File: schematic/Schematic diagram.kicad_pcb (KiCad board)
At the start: 2 copper layers, 23 parts, among them U1 MP4050

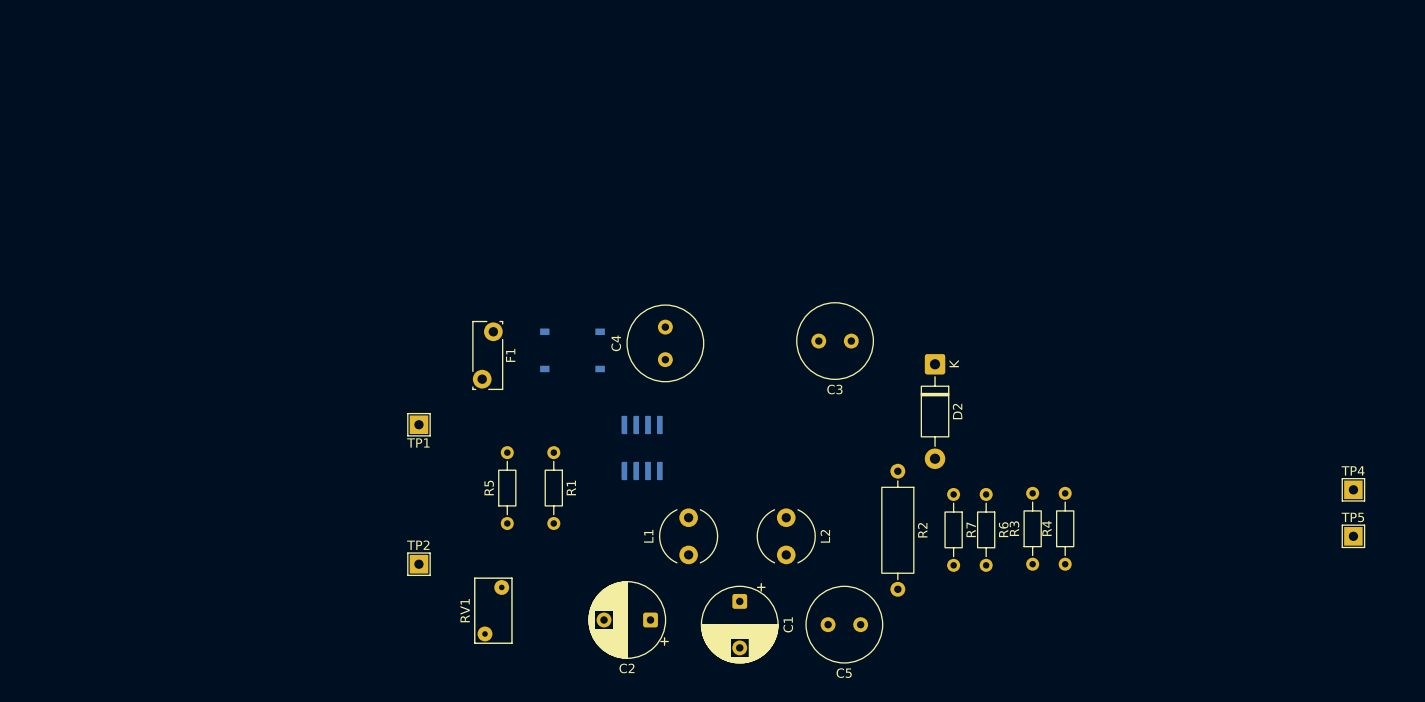
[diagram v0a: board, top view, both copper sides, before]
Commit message: Update PCB routing and improve .gitignore
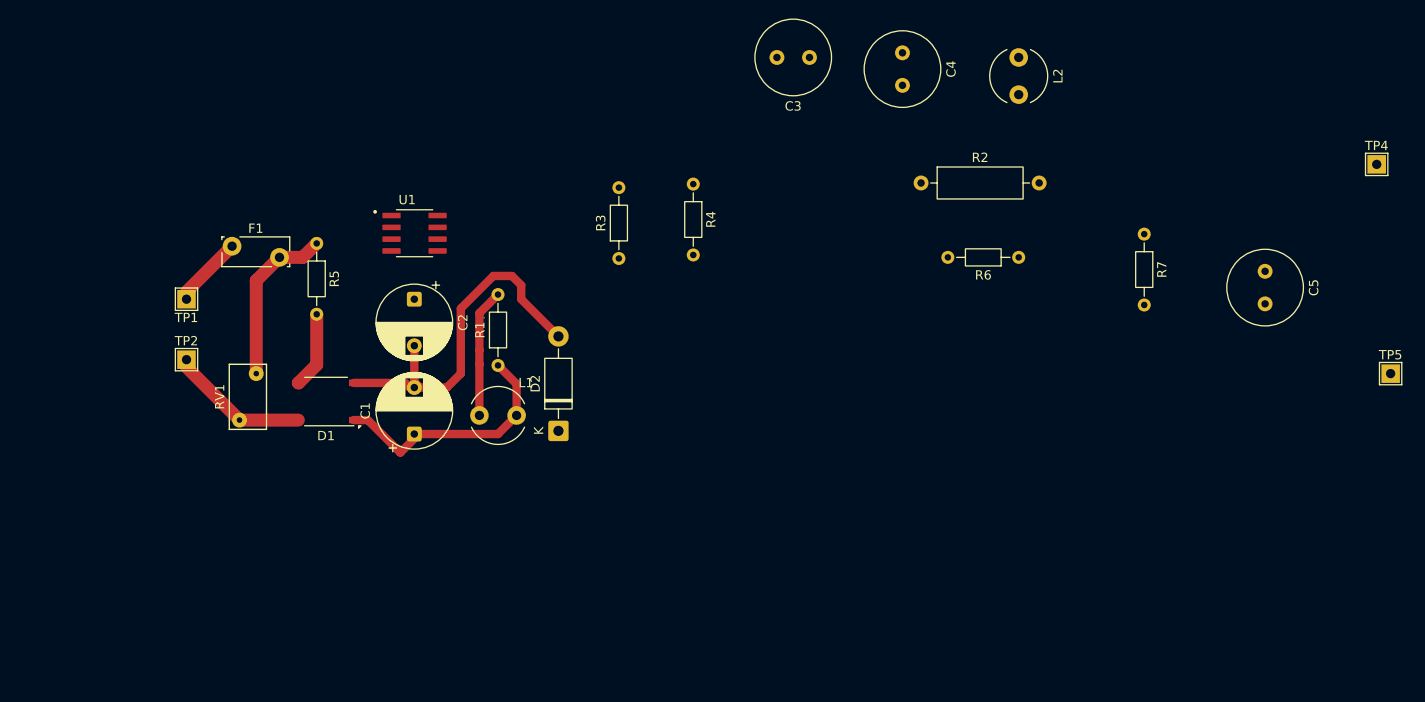
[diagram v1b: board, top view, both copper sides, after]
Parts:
- D1, U1: moved to F.Cu
- moved C5 57.8 mm to (178.0, 93.5), turned to -90 degrees
- moved R4 57.2 mm to (116.5, 84.1), turned to -90 degrees
- moved L2 55.5 mm to (151.5, 70.5)
- moved R3 55.3 mm to (108.5, 92.1)
- moved C2 42.8 mm to (86.5, 96.5), turned to -90 degrees
- moved C4 41.7 mm to (139.0, 70.0), turned to -90 degrees
- moved D2 41.1 mm to (102.0, 110.7), turned to 90 degrees
- moved C1 39.4 mm to (86.5, 111.0), turned to 90 degrees
- moved R5 36.4 mm to (76.0, 90.5), turned to -90 degrees
- moved TP4 35.1 mm to (190.0, 82.0)
- moved RV1 35.0 mm to (69.5, 104.5)
- moved R7 34.7 mm to (165.0, 89.5)
- moved U1 33.7 mm to (86.5, 89.4), turned to 0 degrees
- moved TP2 33.3 mm to (62.0, 103.0)
- moved R2 31.1 mm to (141.0, 84.0), turned to 0 degrees
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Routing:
- net Net-(D1--): track 0.00 -> 41.2 mm
- net Net-(D1-+): track 0.00 -> 27.3 mm
- net Net-(F1-Pad2): track 0.00 -> 18.2 mm
- net Net-(D1-Pad4): track 0.00 -> 15.2 mm
- net Net-(U1-DRAIN): track 0.00 -> 14.3 mm
- net Net-(D1-Pad3): track 0.00 -> 8.21 mm
- net Net-(F1-Pad1): track 0.00 -> 7.73 mm

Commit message: Update PCB routing and add LED schematic, layout and 3D images
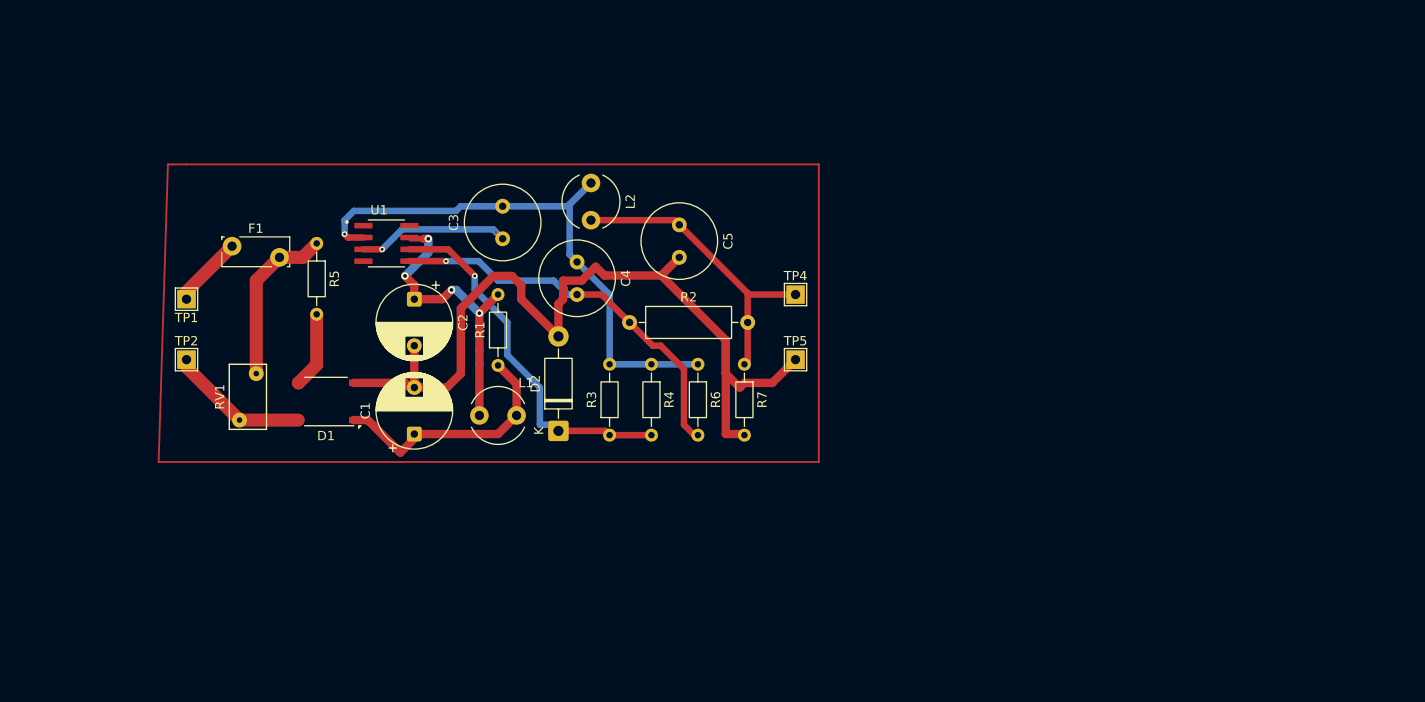
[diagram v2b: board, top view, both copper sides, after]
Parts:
- moved TP4 64.0 mm to (127.5, 96.0)
- moved TP5 64.0 mm to (127.5, 103.0)
- moved C5 63.2 mm to (115.0, 88.5)
- moved L2 47.9 mm to (105.5, 84.0)
- moved R7 45.2 mm to (122.0, 103.5)
- moved C4 41.6 mm to (104.0, 92.5)
- moved C3 38.3 mm to (96.0, 90.0), turned to 90 degrees
- moved R6 36.4 mm to (117.0, 103.5), turned to -90 degrees
- moved R2 34.8 mm to (109.7, 99.0)
- moved R4 19.9 mm to (112.0, 103.5)
- moved R3 19.0 mm to (107.5, 111.1)
- moved U1 3.22 mm to (83.5, 90.5)
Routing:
- net Net-(U1-GND): track 0.00 -> 63.6 mm, vias 0 -> 1
- net Net-(D1--): track 41.2 -> 96.7 mm
- net Net-(U1-PRO): track 0.00 -> 42.4 mm, vias 0 -> 1
- net Net-(D2-K): track 0.00 -> 39.6 mm, vias 0 -> 1
- net Net-(C5-Pad1): track 0.00 -> 33.5 mm
- net Net-(U1-DRAIN): track 14.3 -> 32.1 mm, vias 0 -> 4
- net Net-(U1-VCC): track 0.00 -> 17.3 mm, vias 0 -> 1

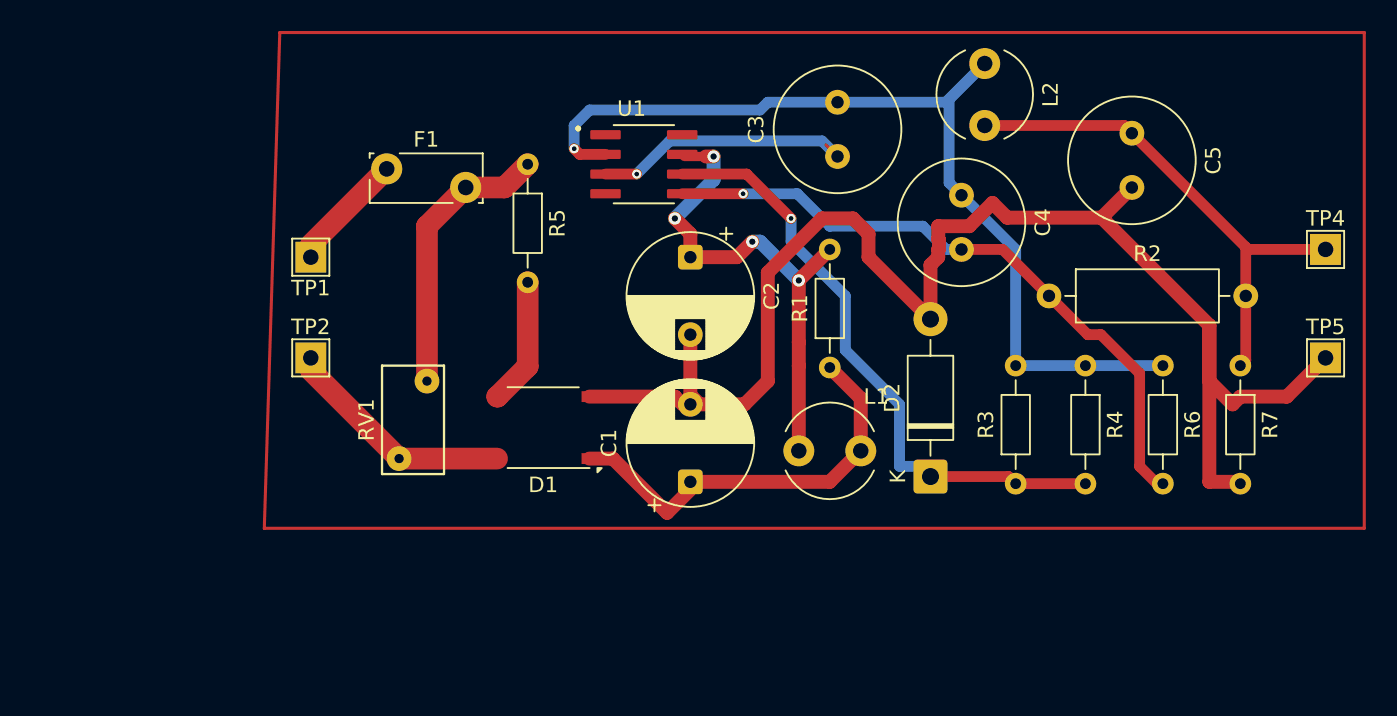
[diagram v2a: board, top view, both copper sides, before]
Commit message: Update PCB design and proteus bridge rectifier simulation
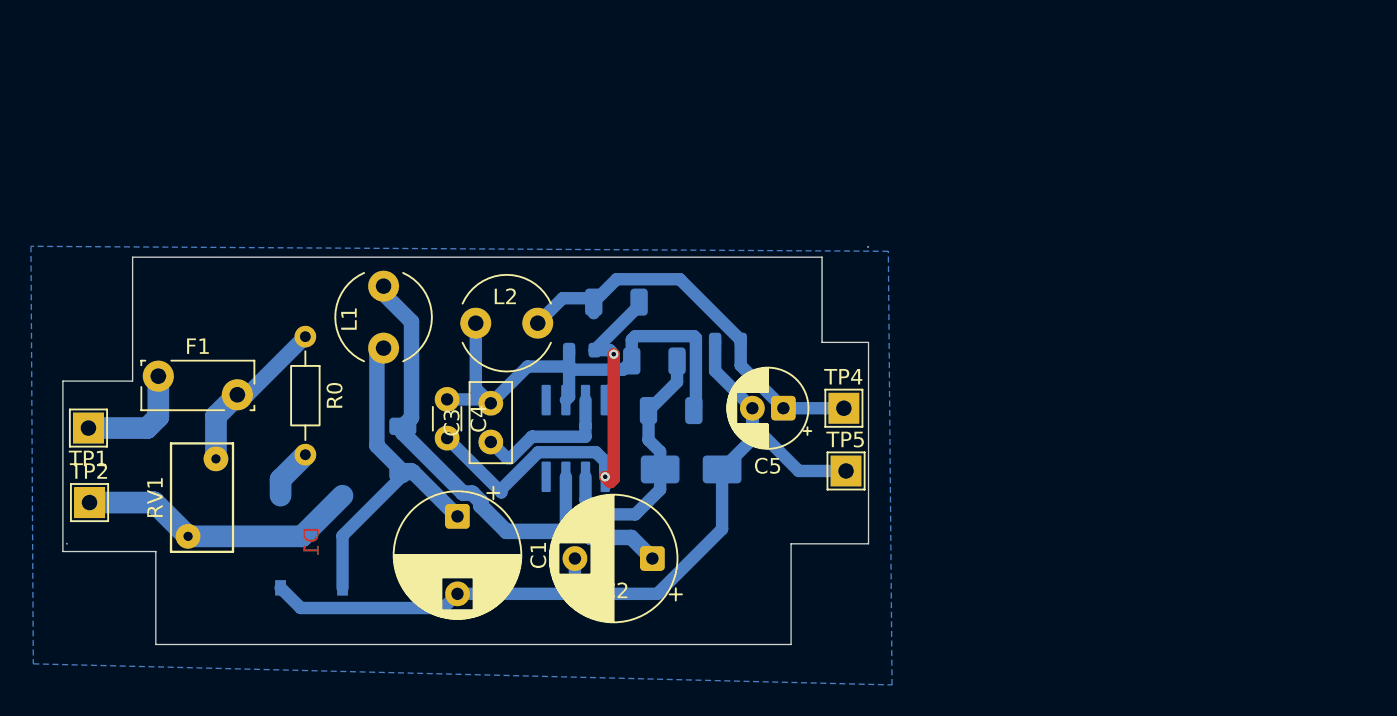
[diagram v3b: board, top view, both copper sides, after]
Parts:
- C3: footprint Capacitor_THT:C_Radial_D8.0mm_H11.5mm_P3.50mm -> Capacitor_THT:C_Disc_D5.0mm_W2.5mm_P2.50mm
- C4: footprint Capacitor_THT:C_Radial_D8.0mm_H11.5mm_P3.50mm -> Capacitor_THT:C_Disc_D3.0mm_W1.6mm_P2.50mm
- C5: footprint Capacitor_THT:C_Radial_D8.0mm_H11.5mm_P3.50mm -> Capacitor_THT:CP_Radial_D5.0mm_P2.00mm
- D1, U1: moved to B.Cu
- D2: footprint Diode_THT:D_DO-41_SOD81_P10.16mm_Horizontal -> Diode_SMD:D_SMA; moved to B.Cu
- R1: renamed from R6; footprint Resistor_THT:R_Axial_DIN0204_L3.6mm_D1.6mm_P7.62mm_Horizontal -> Resistor_SMD:R_0603_1608Metric; moved to B.Cu
- R2: footprint Resistor_THT:R_Axial_DIN0309_L9.0mm_D3.2mm_P12.70mm_Horizontal -> Resistor_SMD:R_1206_3216Metric; moved to B.Cu
- R3, R4: footprint Resistor_THT:R_Axial_DIN0204_L3.6mm_D1.6mm_P7.62mm_Horizontal -> Resistor_SMD:R_1206_3216Metric; moved to B.Cu
- R5: renamed from R1; footprint Resistor_THT:R_Axial_DIN0204_L3.6mm_D1.6mm_P7.62mm_Horizontal -> Resistor_SMD:R_1206_3216Metric; moved to B.Cu
- R6: renamed from R7; footprint Resistor_THT:R_Axial_DIN0204_L3.6mm_D1.6mm_P7.62mm_Horizontal -> Resistor_SMD:R_0603_1608Metric; moved to B.Cu
- moved R1 37.5 mm to (79.5, 102.5), turned to 0 degrees
- moved L2 36.9 mm to (72.7, 100.8), turned to 0 degrees
- moved C4 35.7 mm to (70.8, 105.7)
- moved R6 33.1 mm to (88.9, 101.8), turned to 180 degrees
- moved TP4 32.7 mm to (96.4, 106.2)
- moved TP5 31.8 mm to (96.5, 110.3)
- moved L1 31.5 mm to (66.7, 102.4), turned to 90 degrees
- moved C3 29.0 mm to (73.6, 108.4)
- moved C5 28.7 mm to (92.5, 106.2), turned to 180 degrees
- moved R5 28.1 mm to (67.9, 108.9)
- moved R2 27.9 mm to (81.7, 99.4), turned to 180 degrees
- moved R4 26.9 mm to (85.3, 106.4), turned to 180 degrees
- moved R3 24.6 mm to (84.2, 103.2), turned to 180 degrees
- moved F1 19.9 mm to (52.2, 104.2)
- moved C2 19.6 mm to (84.0, 116.0), turned to 180 degrees
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- renumbered R5 to R0
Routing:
- net Net-(D1--): track 96.7 -> 55.8 mm
- net Net-(U1-GND): track 63.6 -> 32.7 mm, vias 1 -> 0
- net Net-(D2-K): track 39.6 -> 16.8 mm, vias 1 -> 0
- net Net-(U1-PRO): track 42.4 -> 28.5 mm, vias 1 -> 2
- net Net-(U1-VCC): track 17.3 -> 9.48 mm, vias 1 -> 0
- net Net-(F1-Pad2): track 18.2 -> 10.7 mm
- net Net-(C5-Pad1): track 33.5 -> 26.1 mm
- net Net-(D1-Pad3): track 8.21 -> 3.31 mm
- net Net-(D1-+): track 27.3 -> 22.4 mm
- net Net-(D1-Pad4): track 15.2 -> 18.3 mm
- net Net-(U1-DRAIN): track 32.1 -> 33.9 mm, vias 4 -> 0
- added copper zone on B.Cu, net Net-(U1-GND)
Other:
- board outline added: 52 x 25.7 mm

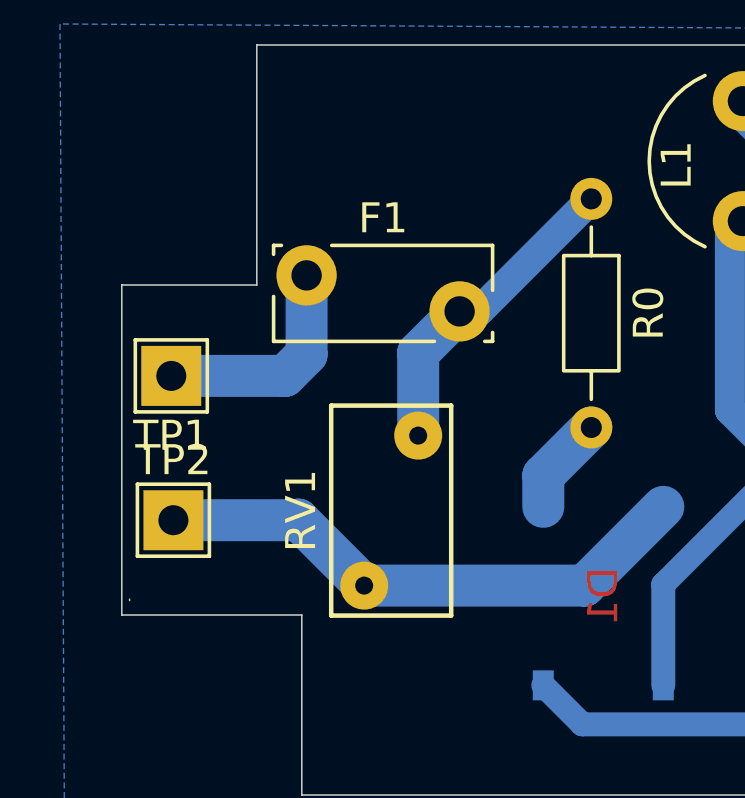
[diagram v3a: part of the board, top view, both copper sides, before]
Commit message: Add PCB fabrication images and update KiCAD project
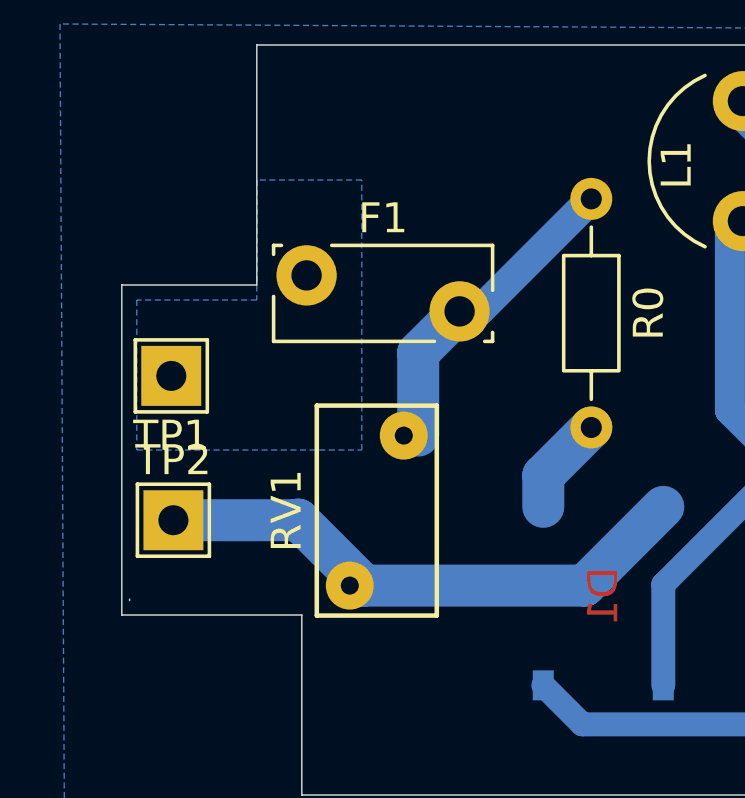
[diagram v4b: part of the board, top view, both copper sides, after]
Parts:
- moved RV1 0.48 mm to (55.4, 109.5)
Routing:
- net Net-(F1-Pad1): track 7.44 -> 0.00 mm
- added copper zone on B.Cu, net Net-(F1-Pad1)
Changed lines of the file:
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@@
 	(footprint "Varistor:RV_Disc_D7mm_W4mm_P5mm"
 		(layer "F.Cu")
-		(at 55.88 109.52 -90)
+		(at 55.4 109.52 -90)
 		(descr "Varistor, diameter 7mm, width 4mm, pitch 5mm")
 		(tags "varistor SIOV")
@@
 	)
 	(segment
-		(start 52.16 106.81)
-		(end 52.16 104.18)
-		(width 1.4)
-		(layer "B.Cu")
-		(net "Net-(F1-Pad1)")
-	)
-	(segment
-		(start 51.44 107.53)
-		(end 52.16 106.81)
-		(width 1.4)
-		(layer "B.Cu")
-		(net "Net-(F1-Pad1)")
-	)
-	(segment
-		(start 47.65 107.53)
-		(end 51.44 107.53)
-		(width 1.4)
-		(layer "B.Cu")
-		(net "Net-(F1-Pad1)")
-	)
-	(segment
 		(start 72.42043 111.73)
 		(end 72.97 112.27957)
@@
 		(name "GND")
 		(hatch edge 0.5)
-		(priority 1)
 		(connect_pads
 			(clearance 0.5)
 		)
 		(min_thickness 0.25)
-		(fill
+		(fill yes
 			(thermal_gap 0.5)
 			(thermal_bridge_width 0.5)
@@
 			)
 		)
+	)
+	(zone
+		(net "Net-(F1-Pad1)")
+		(layer "B.Cu")
+		(hatch edge 0.5)
+		(priority 1)
+		(connect_pads
+			(clearance 0.3)
+		)
+		(min_thickness 0.25)
+		(fill yes
+			(thermal_gap 0.5)
+			(thermal_bridge_width 0.5)
+			(island_removal_mode 0)
+		)
+		(polygon
+			(pts
+				(xy 46.5 105) (xy 46.5 110) (xy 54 110) (xy 54 101) (xy 50.5 101) (xy 50.5 105)
+			)
+		)
